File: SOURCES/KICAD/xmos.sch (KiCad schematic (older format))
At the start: 76 parts, among them IC401 IC_NC7WZ07, IC402 NC7SZ175, IC403 IC_XE216-512-TQ128, IC404 IC_CS2100CP, IC405 NC7SZ157, IC406 NC7SZ157, IC407 IC_NCP4681DSQ25T1G, IC408 IC_IS25LP080D, IC409 IC_NCP1117LPST33, IC410 IC_TLV62565, X401 HDR_01x05, X402 CON_HDR_02x10

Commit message: Updated BOM
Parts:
- C401: Manufacturer (none) -> Yageo; pn (none) -> CC0805KRX7R9BB103
- C402, C403, C404, C405, C406, C407, C408, C411, C413: Manufacturer (none) -> KEMET; pn (none) -> C0805C104K5RACTU
- C409, C410, C412, C414, C415: Manufacturer (none) -> Murata Electronics North America; pn (none) -> GRM21BR61E106MA73L
- C416: Manufacturer (none) -> Murata Electronics North America; pn (none) -> GRM21BR61A226ME51L
- C417, C418, C419, C420, C421, C422, C423, C424, C425, C426, C427, C428, C429, C430, C431, C432, C433, C434, C435, C436, C437, C438, C439, C440, C441: Manufacturer (none) -> Murata Electronics North America; pn (none) -> GRM155R71A104KA01D
- D401: Manufacturer (none) -> ON Semiconductor; pn (none) -> MBR120VLSFT3G
- IC401: Manufacturer (none) -> ON Semiconductor; pn (none) -> NC7WZ07P6X
- IC402: Manufacturer (none) -> Texas Instruments; pn (none) -> SN74LVC1G175DCKR
- IC403: Manufacturer (none) -> XMOS; pn (none) -> XE216-512-TQ128-C20
- IC404: Manufacturer (none) -> Cirrus Logic Inc.; pn (none) -> CS2100CP-CZZ
- IC405, IC406: Manufacturer (none) -> ON Semiconductor; pn (none) -> NC7SZ157P6X
- IC407: Manufacturer (none) -> ON Semiconductor; pn (none) -> NCP4681DSQ25T1G
- IC408: Manufacturer (none) -> ISSI, Integrated Silicon Solution Inc; pn (none) -> IS25LP080D-JNLE
- IC409: Manufacturer (none) -> ON Semiconductor; pn (none) -> NCP1117LPST33T3G
- IC410: Manufacturer (none) -> Texas Instruments; pn (none) -> TLV62565DBVR
- L401: Manufacturer (none) -> Murata Power Solutions Inc.; pn (none) -> 45222C
- OSC401: Manufacturer (none) -> Abracon LLC; pn (none) -> ASFL1-24.000MHZ-EC-T
- R401, R405, R406, R413, R414: Manufacturer (none) -> Yageo; pn (none) -> RC0805FR-0710KL
- R402, R404, R408, R409, R411, R412: Manufacturer (none) -> Yageo; pn (none) -> RC0805FR-0733RL
- R403: Manufacturer (none) -> Yageo; pn (none) -> RC0805FR-074R7L
- R407: Manufacturer (none) -> Yageo; pn (none) -> TC164-JR-0733RL
- R410: Manufacturer (none) -> Yageo; pn (none) -> RC0805FR-071KL
- R415: Manufacturer (none) -> Panasonic Electronic Components; pn (none) -> ERJ-6ENF43R2V
- R416, R417: Manufacturer (none) -> Yageo; pn (none) -> RC0805FR-072KL
- R418: Manufacturer (none) -> Yageo; pn (none) -> RC0805FR-07100KL
- R419: Manufacturer (none) -> Yageo; pn (none) -> RC0805FR-0780K6L
- R420: Manufacturer (none) -> Yageo; pn (none) -> RC0805FR-07120KL
- X401: Manufacturer (none) -> Sullins Connector Solutions; pn (none) -> PRPC005SAAN-RC
- X402: Manufacturer (none) -> Sullins Connector Solutions; pn (none) -> PRPC010DAAN-RC

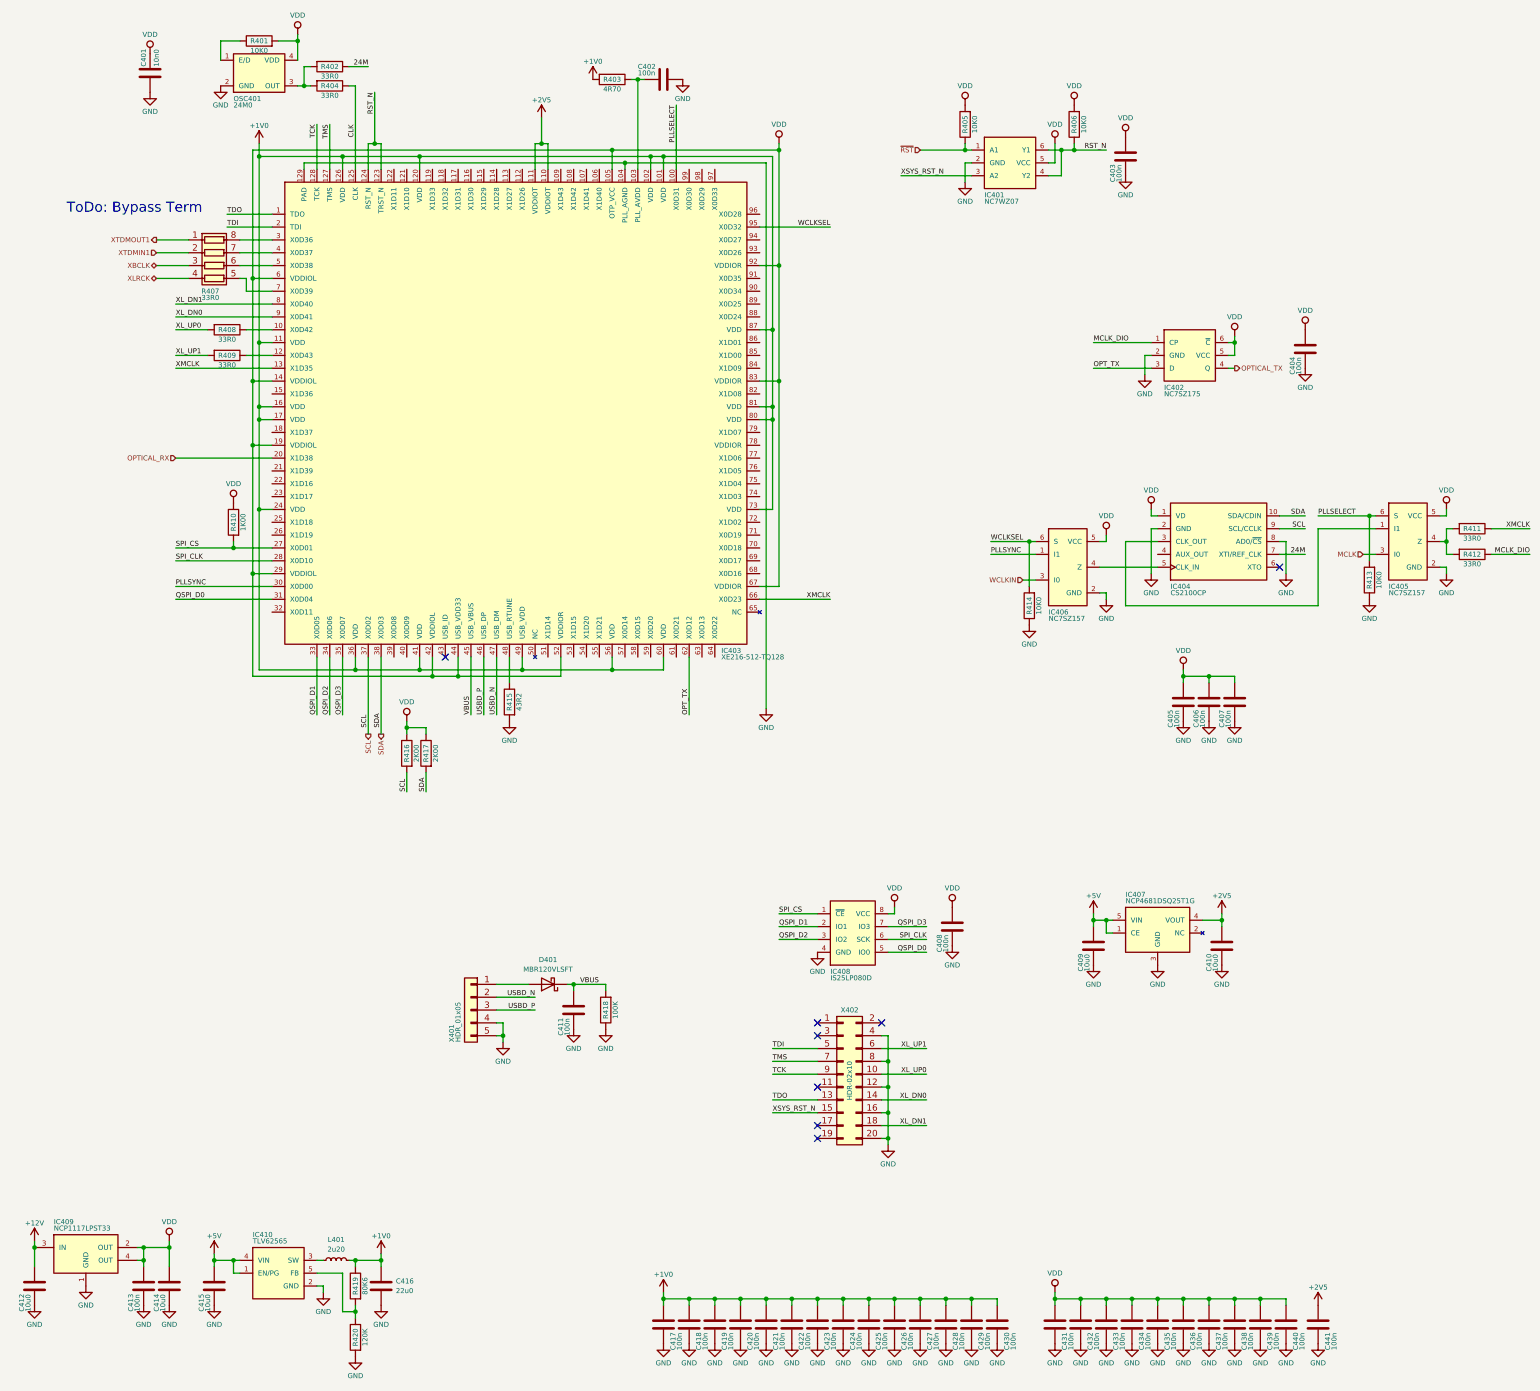
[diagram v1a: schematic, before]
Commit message: Updated sendParameter
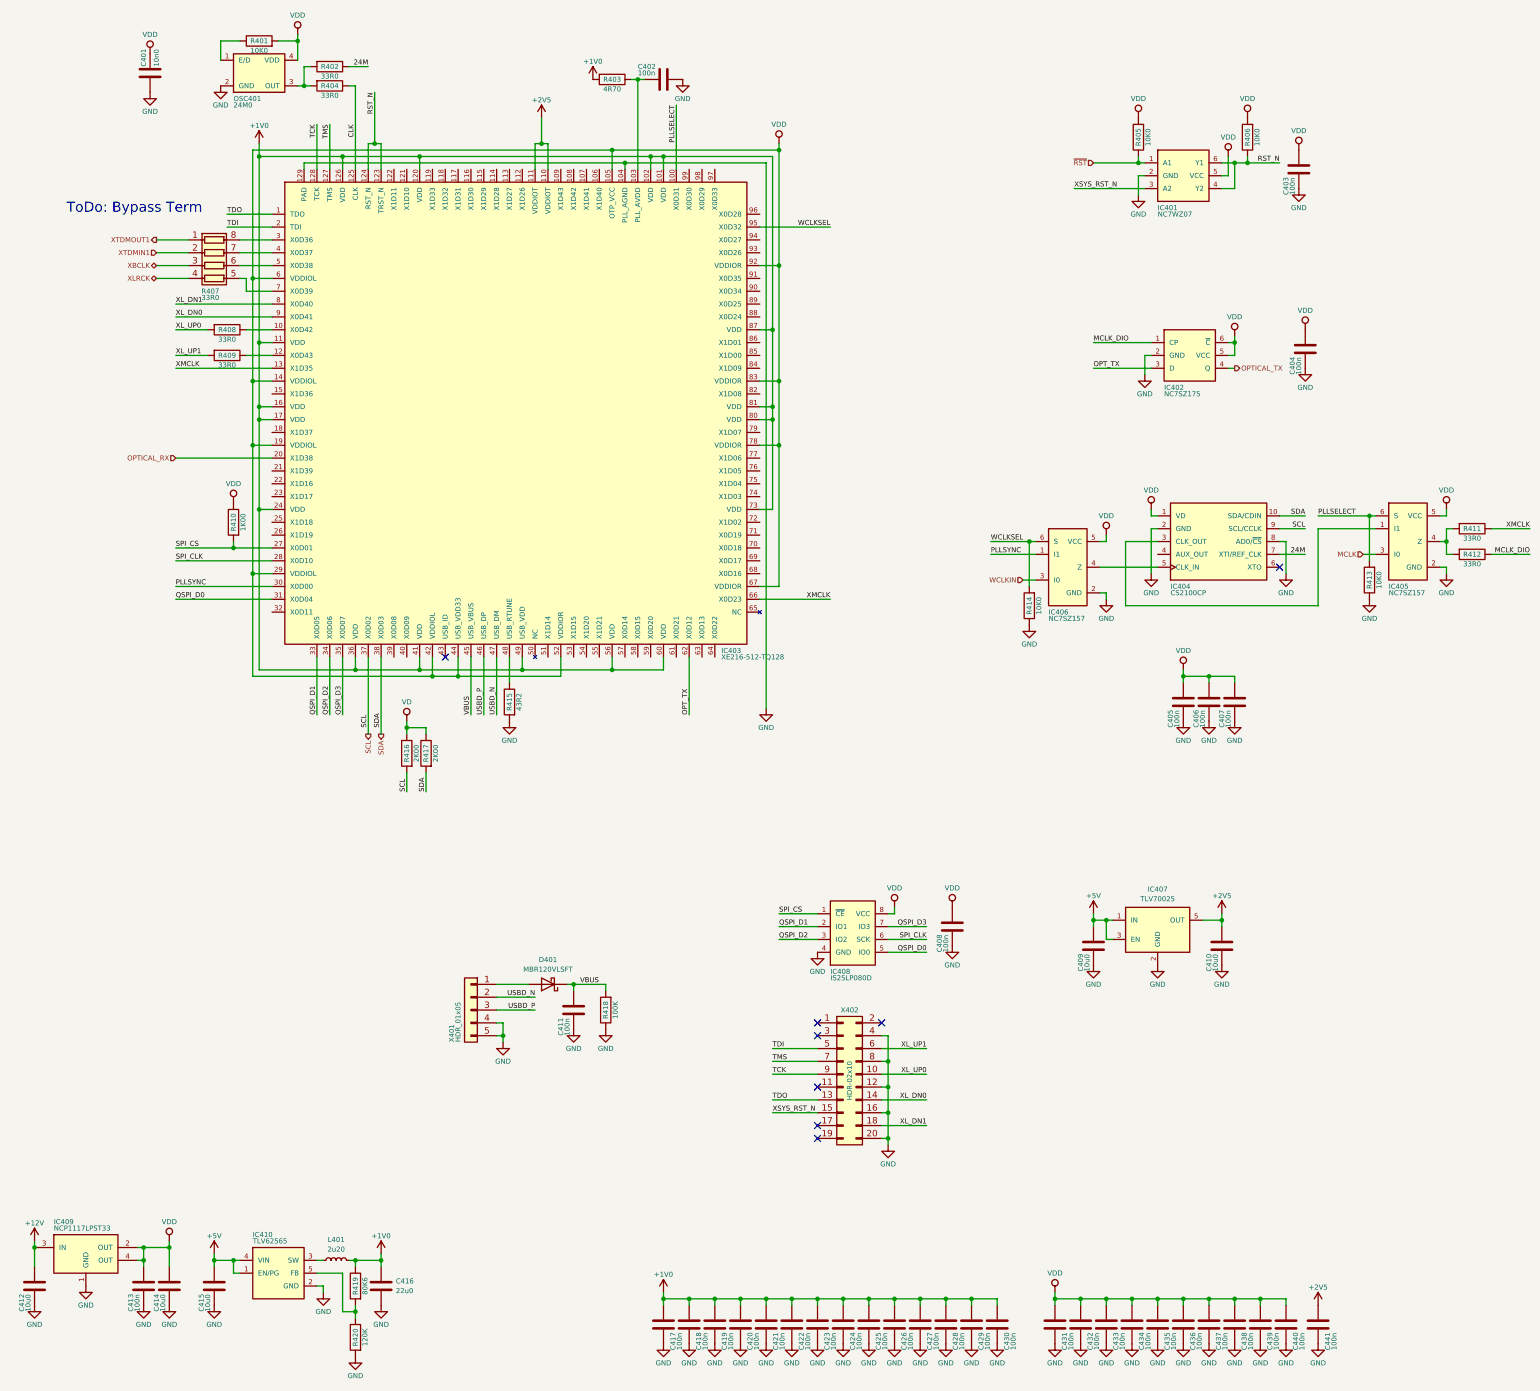
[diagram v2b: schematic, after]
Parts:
- removed IC407: IC_NCP4681DSQ25T1G, TO_SOT_Packages_SMD:SC-70-5, symbol rk:IC_NCP4681DSQ25T1G
- added IC407: TLV70025, rklib:SC70-5, symbol rkdev:TLV70025
- IC402: digikey ??? -> 296-16998-1-ND
- R407: digikey ??? -> TC164J-33CT-ND
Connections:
- net +2V5: now also IC407.5 (OUT)
- net +5V: now also IC407.1 (IN), IC407.3 (EN)
- net GND: now also IC407.2 (GND)
- net VDD: now also IC403.78 (VDDIOR); no longer R416.1, R417.1
- new net VD: R416.1, R417.1
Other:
- moved on the sheet: C403, IC401, R405, R406

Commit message: Bugfix: Made WiFi pins unconnected
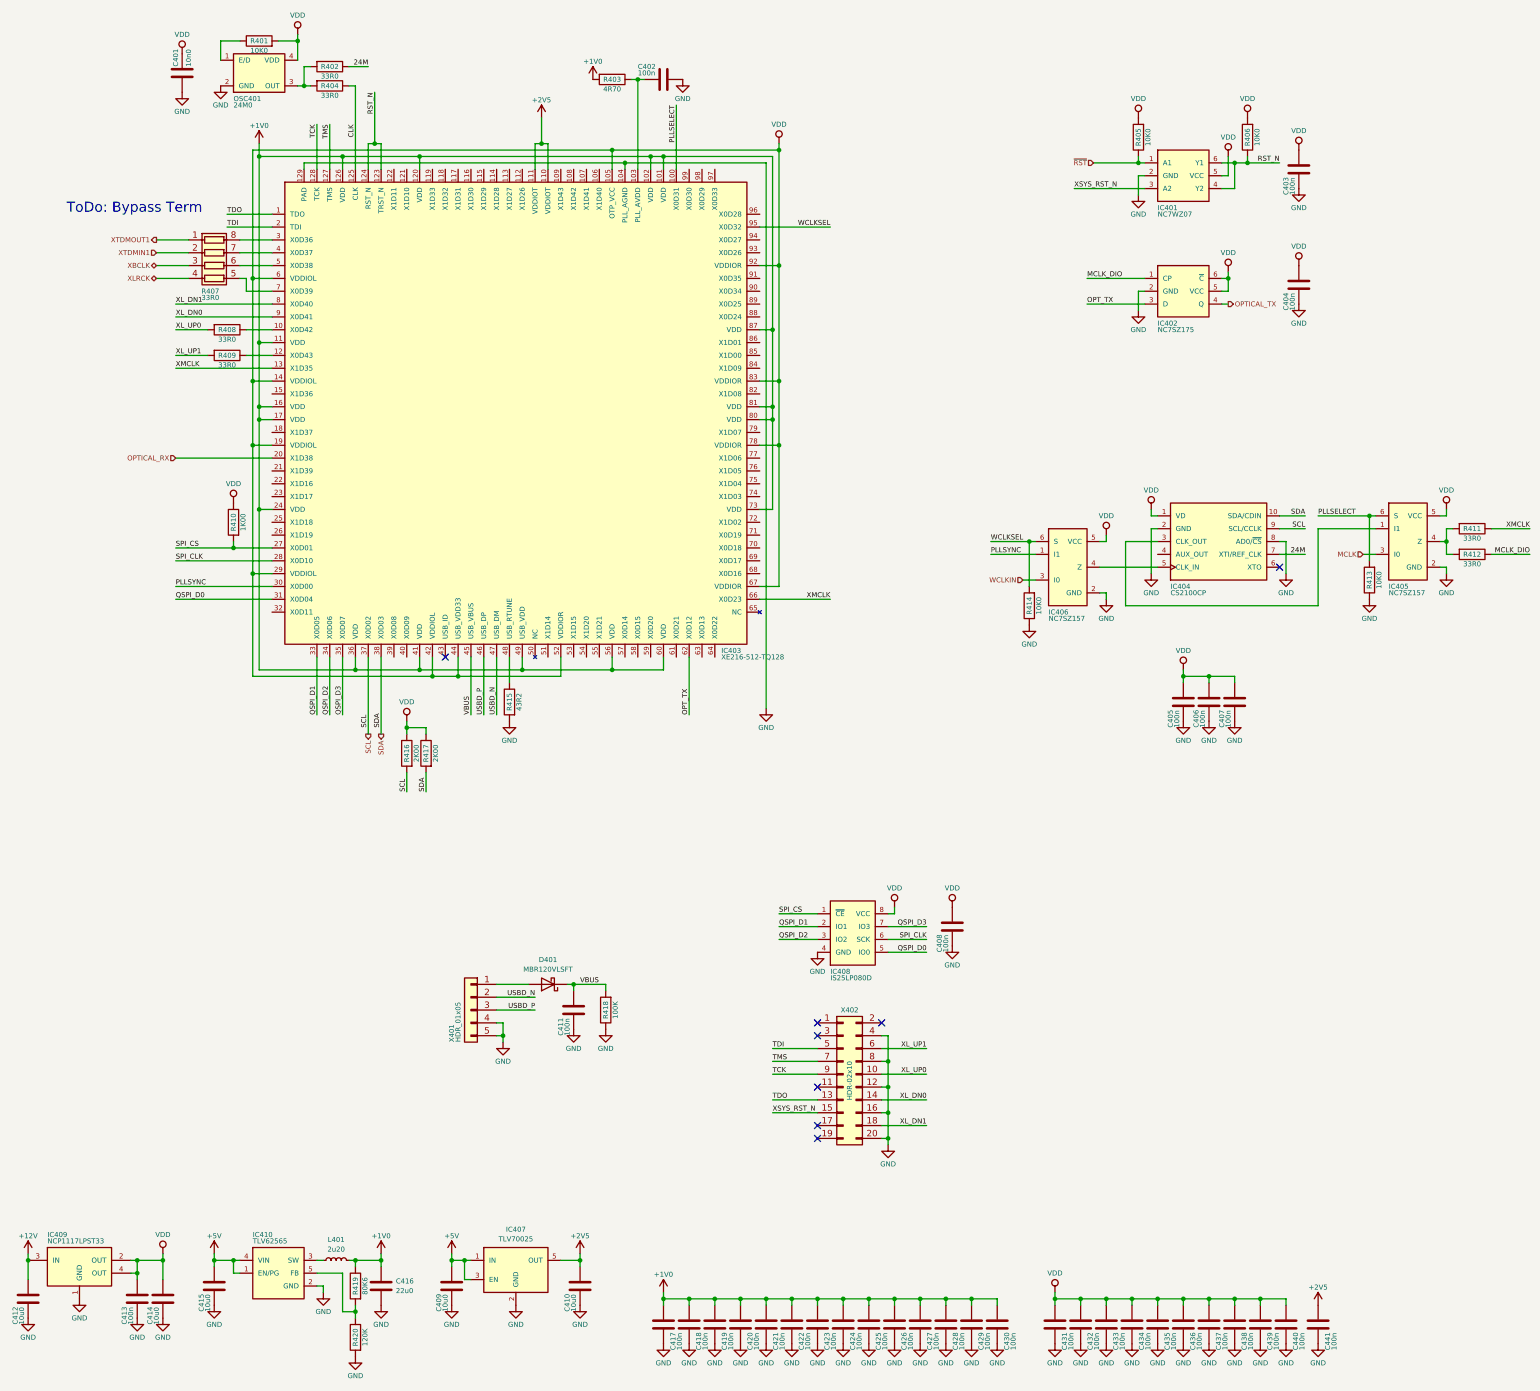
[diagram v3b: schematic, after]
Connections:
- net VD is gone; now on net VDD: R416.1, R417.1
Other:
- moved on the sheet: C401, C404, C409, C410, C412, C413, C414, IC402, IC407, IC409

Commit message: Minor bugfixes on hardware
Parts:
- added R421: RES_10K0_1%_0.125W_Thick_0805, rklib:C0805-RES, symbol freeDSP-aurora-rescue:RES_10K0_1%_0.25W_Thin_0805
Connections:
- net VDD: now also R421.2
- net XSYS_RST_N: now also R421.1
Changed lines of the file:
@@
 Text HLabel 4150 6100 3    39   Output ~ 0
 SDA
-Text HLabel 9700 1650 0    39   Input ~ 0
+Text HLabel 9650 1650 0    39   Input ~ 0
 ~RST
 $Comp
@@
 	1    0    0    -1
 $EndComp
-Text Label 9550 1850 0    39   ~ 0
+Text Label 9500 1850 0    39   ~ 0
 XSYS_RST_N
 Text Label 11150 1650 2    39   ~ 0
@@
 	4150 1500 4150 1700
 Wire Wire Line
-	9700 1650 10050 1650
+	9650 1650 10050 1650
 Connection ~ 4100 1500
 Wire Wire Line
@@
 	10050 1750 10100 1750
 Wire Wire Line
-	9550 1850 10100 1850
+	9500 1850 9900 1850
 Wire Wire Line
 	10700 1650 10800 1650
@@
 	1    0    0    -1
 $EndComp
+$Comp
+L freeDSP-aurora-rescue:VDD #PWR0401
+U 1 1 5DB93C2B
+P 9900 1300
+F 0 "#PWR0401" H 9900 1150 50  0001 C CNN
+F 1 "VDD" H 9900 1450 39  0000 C CNN
+F 2 "" H 9900 1300 50  0000 C CNN
+F 3 "" H 9900 1300 50  0000 C CNN
+	1    9900 1300
+	1    0    0    -1
+$EndComp
+$Comp
+L freeDSP-aurora-rescue:RES_10K0_1%_0.25W_Thin_0805 R421
+U 1 1 5DB93C36
+P 9900 1450
+F 0 "R421" H 9900 1450 39  0000 C CNN
+F 1 "RES_10K0_1%_0.125W_Thick_0805" H 9900 1275 39  0001 C CNN
+F 2 "rklib:C0805-RES" H 9900 1225 39  0001 C CNN
+F 3 "" H 9900 1450 50  0000 C CNN
+F 4 "10K0" H 9900 1375 39  0000 C CNN "Value1"
+F 5 "1% 0.125W Thick" H 9900 1325 39  0001 C CNN "Value2"
+F 6 "311-10.0KCRCT-ND" H 9900 1150 39  0001 C CNN "digikey"
+F 7 "Yageo" H 1200 100 50  0001 C CNN "Manufacturer"
+F 8 "RC0805FR-0710KL" H 1200 100 50  0001 C CNN "pn"
+	1    9900 1450
+	0    -1   -1   0
+$EndComp
+Wire Wire Line
+	9900 1600 9900 1850
+Connection ~ 9900 1850
+Wire Wire Line
+	9900 1850 10100 1850
 $EndSCHEMATC
